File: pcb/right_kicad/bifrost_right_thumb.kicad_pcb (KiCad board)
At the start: 2 copper layers, 44.8 x 20.8 mm, 9 parts, among them J1 Conn_01x05, SW1 1U, SW2 1U

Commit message: Update PCB and case designs
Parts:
- moved H2 56.1 mm to (109.0, 59.8)
- moved J1 56.1 mm to (96.7, 50.4)
- moved C1 56.1 mm to (80.3, 65.7)
- moved C2 56.1 mm to (99.2, 64.7)
- moved D1 56.1 mm to (81.0, 65.6)
- moved SW2 56.1 mm to (99.2, 59.5)
- moved D2 56.1 mm to (99.9, 64.7)
- moved H1 56.1 mm to (89.5, 59.8)
- moved SW1 56.1 mm to (79.8, 60.6)
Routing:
- net GND: vias 0 -> 63

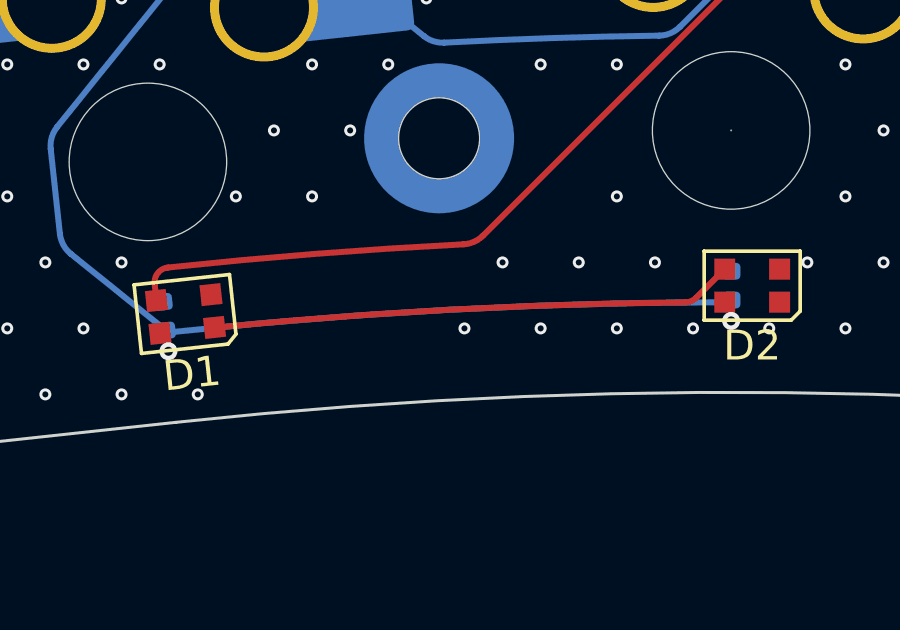
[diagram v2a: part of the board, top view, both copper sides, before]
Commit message: Update PCB fabrication outputs and switch knob
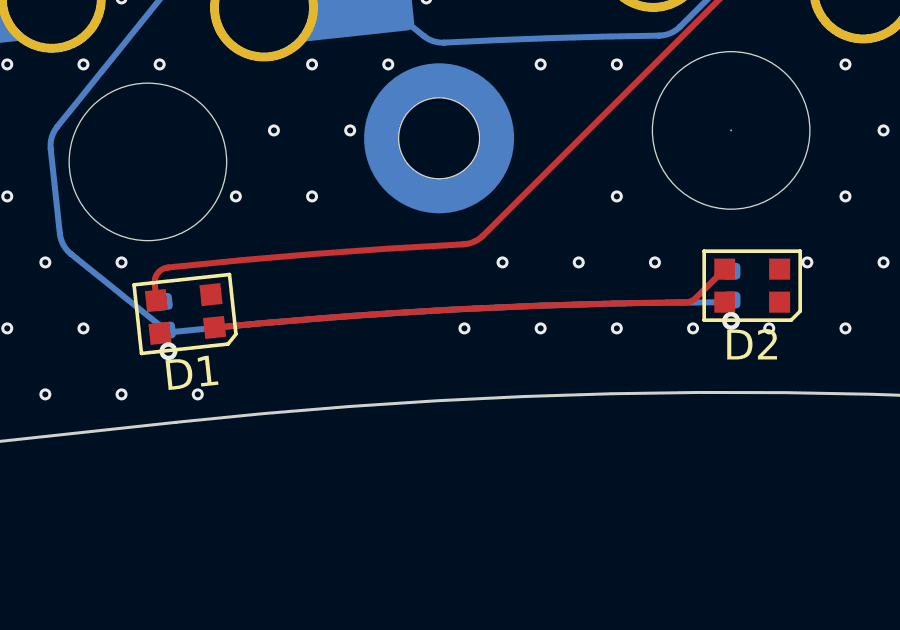
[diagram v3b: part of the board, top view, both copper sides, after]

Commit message: Update PCB designs and fabrication outputs
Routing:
- net RGB_PWR: track 53.9 -> 54.7 mm

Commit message: Update PCB layouts and production files
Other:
- board text added: "Bifrost rev.1.0"

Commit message: Update Bifrost case and PCB outputs
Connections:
- J1 pad 2: RGB -> GND
- J1 pad 3: GND -> RGB

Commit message: Update PCB mounting hardware footprints
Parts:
- D1, D2: value WS2812B-2020 -> WS2812C-2020
- H1, H2: footprint Smidr:MountingHole_TH-1.6-M2 -> Smidr:SMD-1_BD4.4-D2.8
- turned H1 to 0 degrees
- turned H2 to 0 degrees
